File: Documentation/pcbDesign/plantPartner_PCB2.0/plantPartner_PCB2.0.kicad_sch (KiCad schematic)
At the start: 52 parts, among them IC1 MPM3610, J1 Conn_01x04, J11 Conn_01x02, J16 Conn_01x04, J17 Conn_01x03, J2 Conn_01x04, J20 Conn_02x04_Top_Bottom, J21 Conn_01x04, J22 Conn_01x04, J23 Conn_01x01, J24 Conn_01x03, J25 Conn_01x03, J26 Conn_01x01, J27 Conn_01x01, J28 Conn_01x01, J29 Conn_01x02, J3 Conn_01x04, J30 Screw_Terminal_01x02, J4 Screw_Terminal, J5 Conn_01x02, J6 Barrel_Jack, J7 Screw_Terminal_01x02, J8 Conn_02x04_Top_Bottom, Q4 AO3400A, U2 MAX485, U3 ESP32-DEVKIT-V1

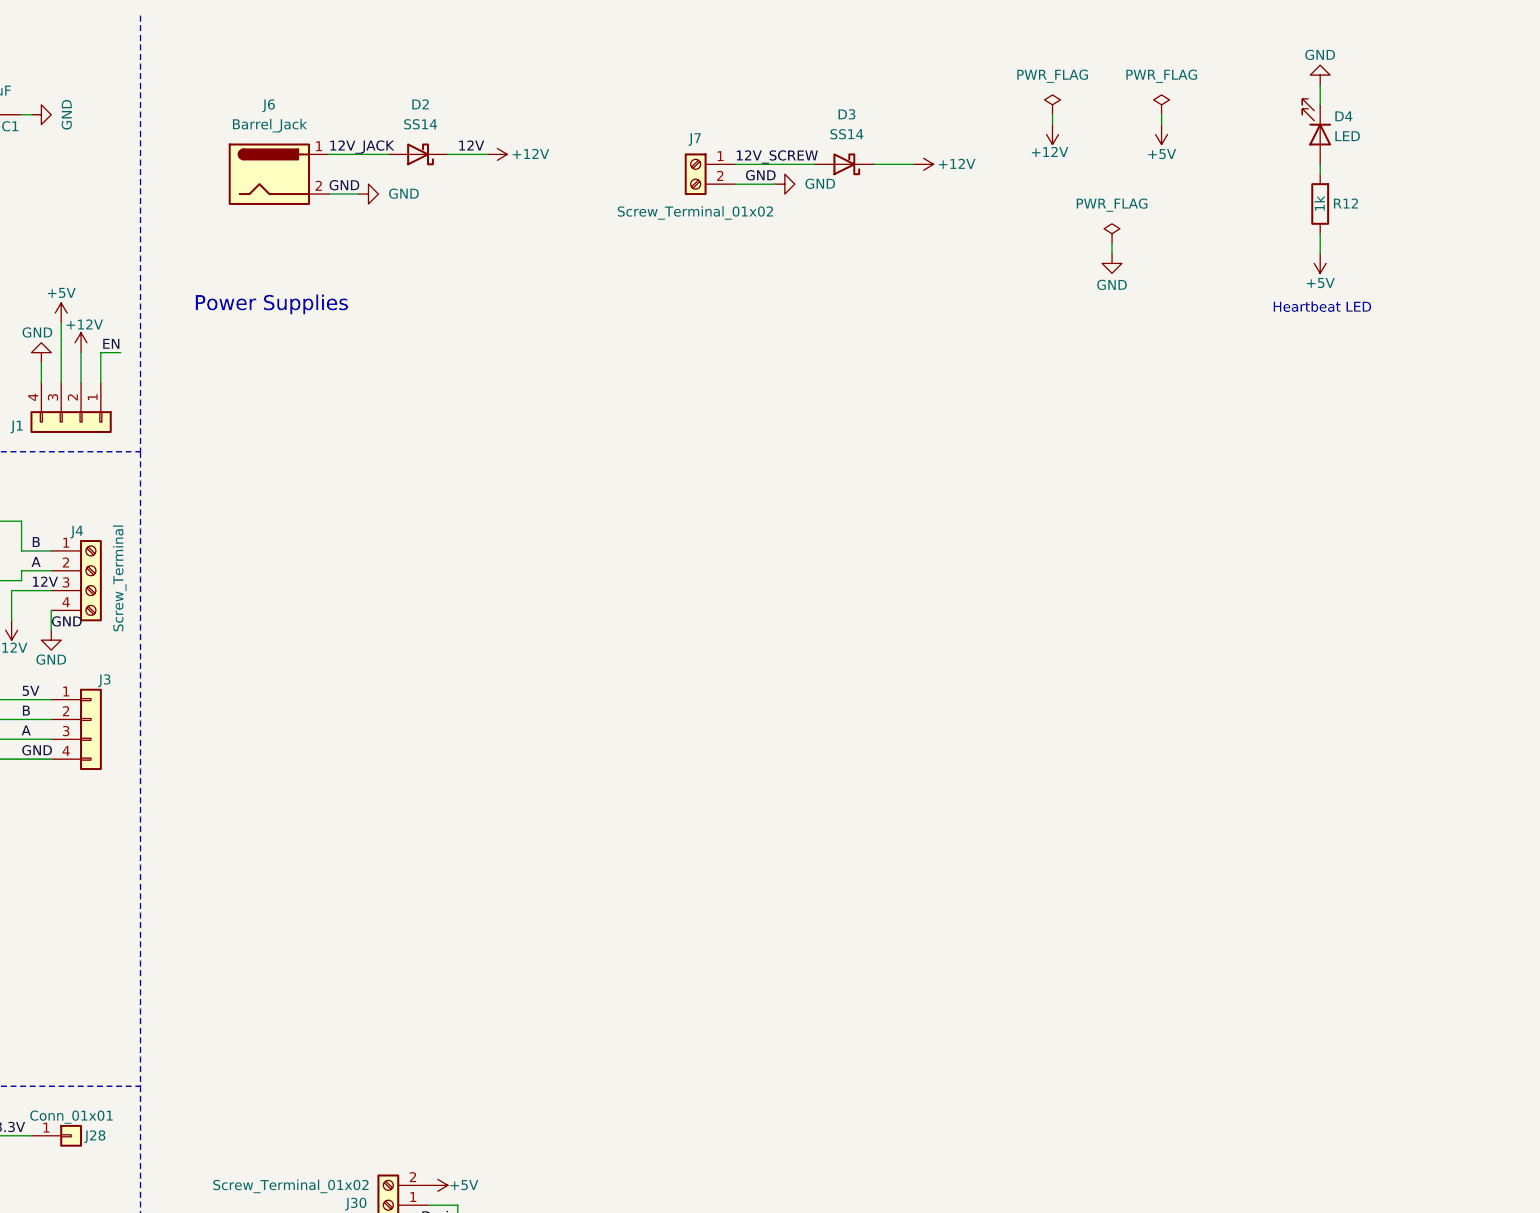
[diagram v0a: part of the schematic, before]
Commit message: Added basic implementation of 2.0 changes to see how much cheaper new PCB would be. As of now, it is half the price :O
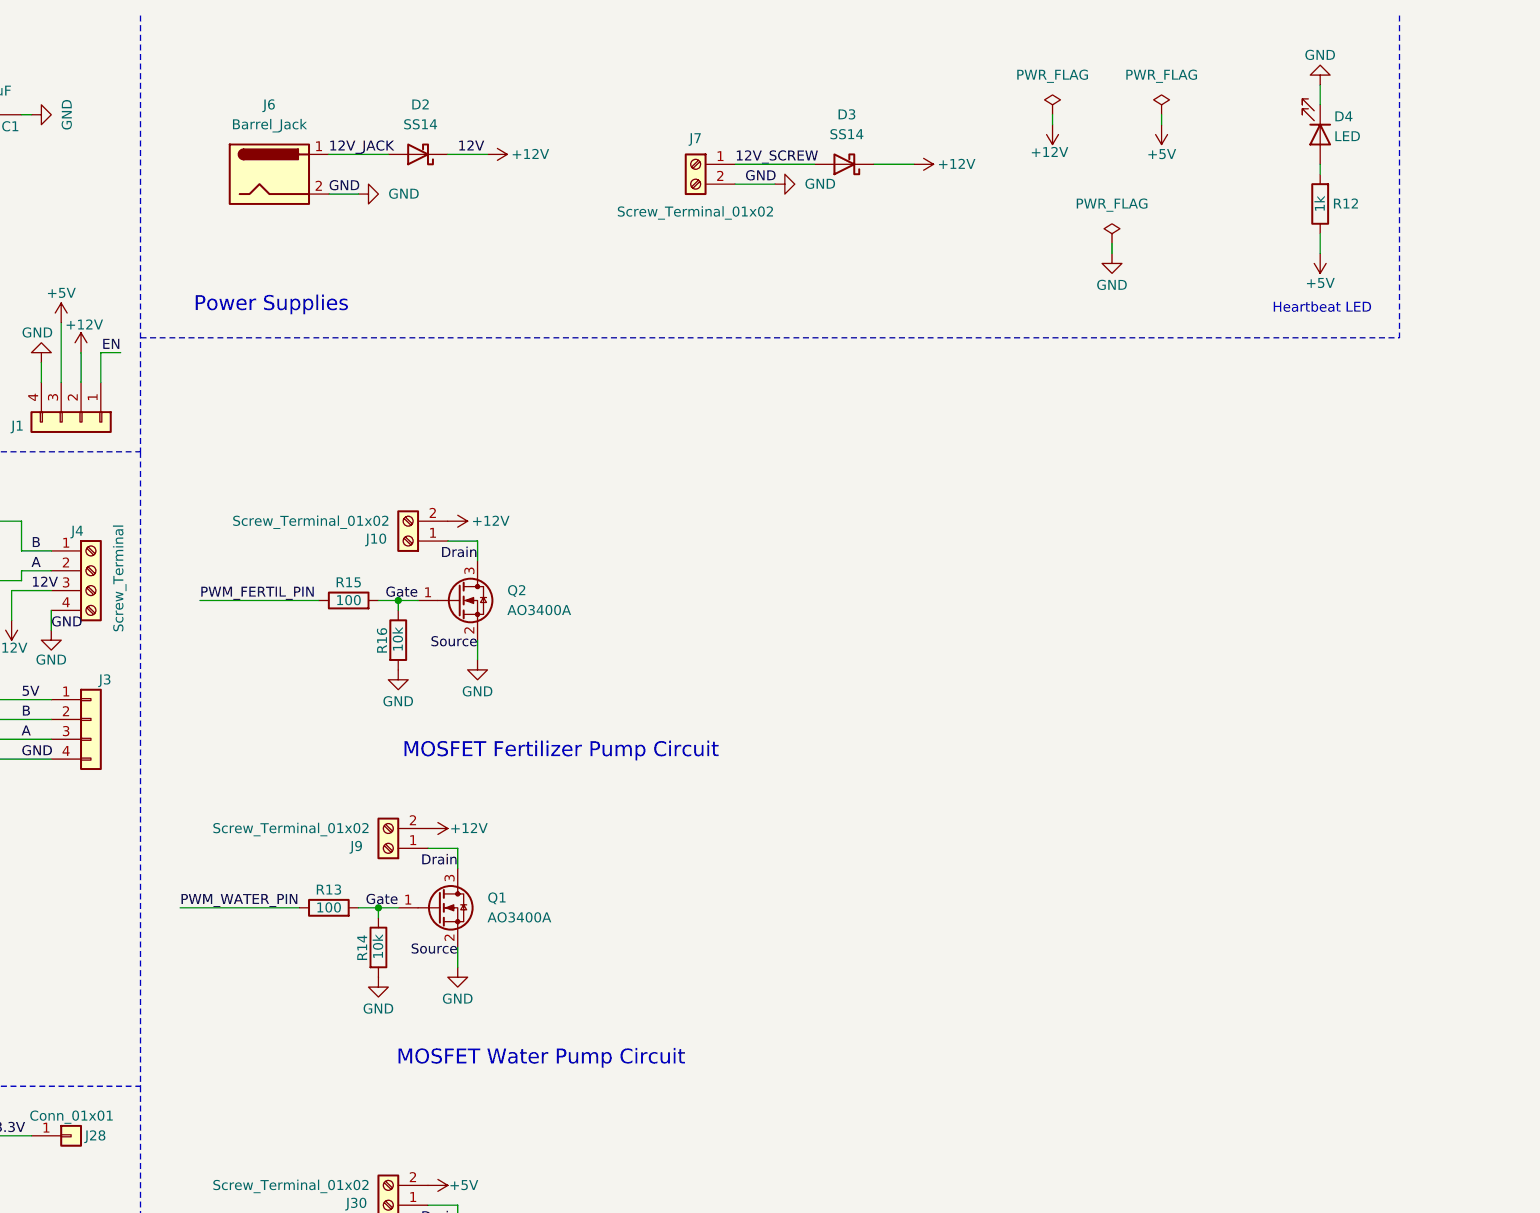
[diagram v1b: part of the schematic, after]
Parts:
- added J10, J9: Screw_Terminal_01x02, TerminalBlock_Phoenix:TerminalBlock_Phoenix_MPT-0,5-2-2.54_1x02_P2.54mm_Horizontal, symbol Connector:Screw_Terminal_01x02
- added Q1, Q2: AO3400A, Package_TO_SOT_SMD:SOT-23, symbol Transistor_FET:AO3400A
- added R13, R15: 100, Resistor_SMD:R_0402_1005Metric, symbol Device:R
- added R14, R16: 10k, Resistor_SMD:R_0402_1005Metric, symbol Device:R
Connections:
- net +12V: now also J10.2 (Pin_2), J9.2 (Pin_2)
- net Drain: now also J10.1 (Pin_1), J9.1 (Pin_1), Q1.3 (D), Q2.3 (D)
- net GND: now also Q1.2 (S), Q2.2 (S), R14.2, R16.2
- net Gate: now also Q1.1 (G), Q2.1 (G), R13.2, R14.1, R15.2, R16.1
- net PWM_FERTIL_PIN: now also R15.1
- net PWM_WATER_PIN: now also R13.1
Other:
- note added: "MOSFET Fertilizer Pump Circuit"
- note added: "MOSFET Water Pump Circuit"

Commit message: Cleaning up MOSFET circuits
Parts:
- added C5, C6: 220uF, Capacitor_SMD:C_0603_1608Metric, symbol Device:C
- added D5, D6: SS14, Diode_SMD:D_SMA, symbol Device:D_Schottky
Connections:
- net +12V: no longer J10.2 (Pin_2), J9.2 (Pin_2)
- net +5V: now also J10.2 (Pin_2), J9.2 (Pin_2), C5.1, C6.1, D5.1 (K), D6.1 (K)
- net Drain: now also D5.2 (A), D6.2 (A)
- net GND: now also C5.2, C6.2
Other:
- note removed: "Terminal Blocks Needed: 2 Pin - 2 * 5 = 10 3 Pin - 2 * 5 = 10 4 Pin - 1 * 5 = 5"
- moved on the sheet: C1, C2, C3, C4, D1, D10, D2, D3, D4, IC1, J1, J10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

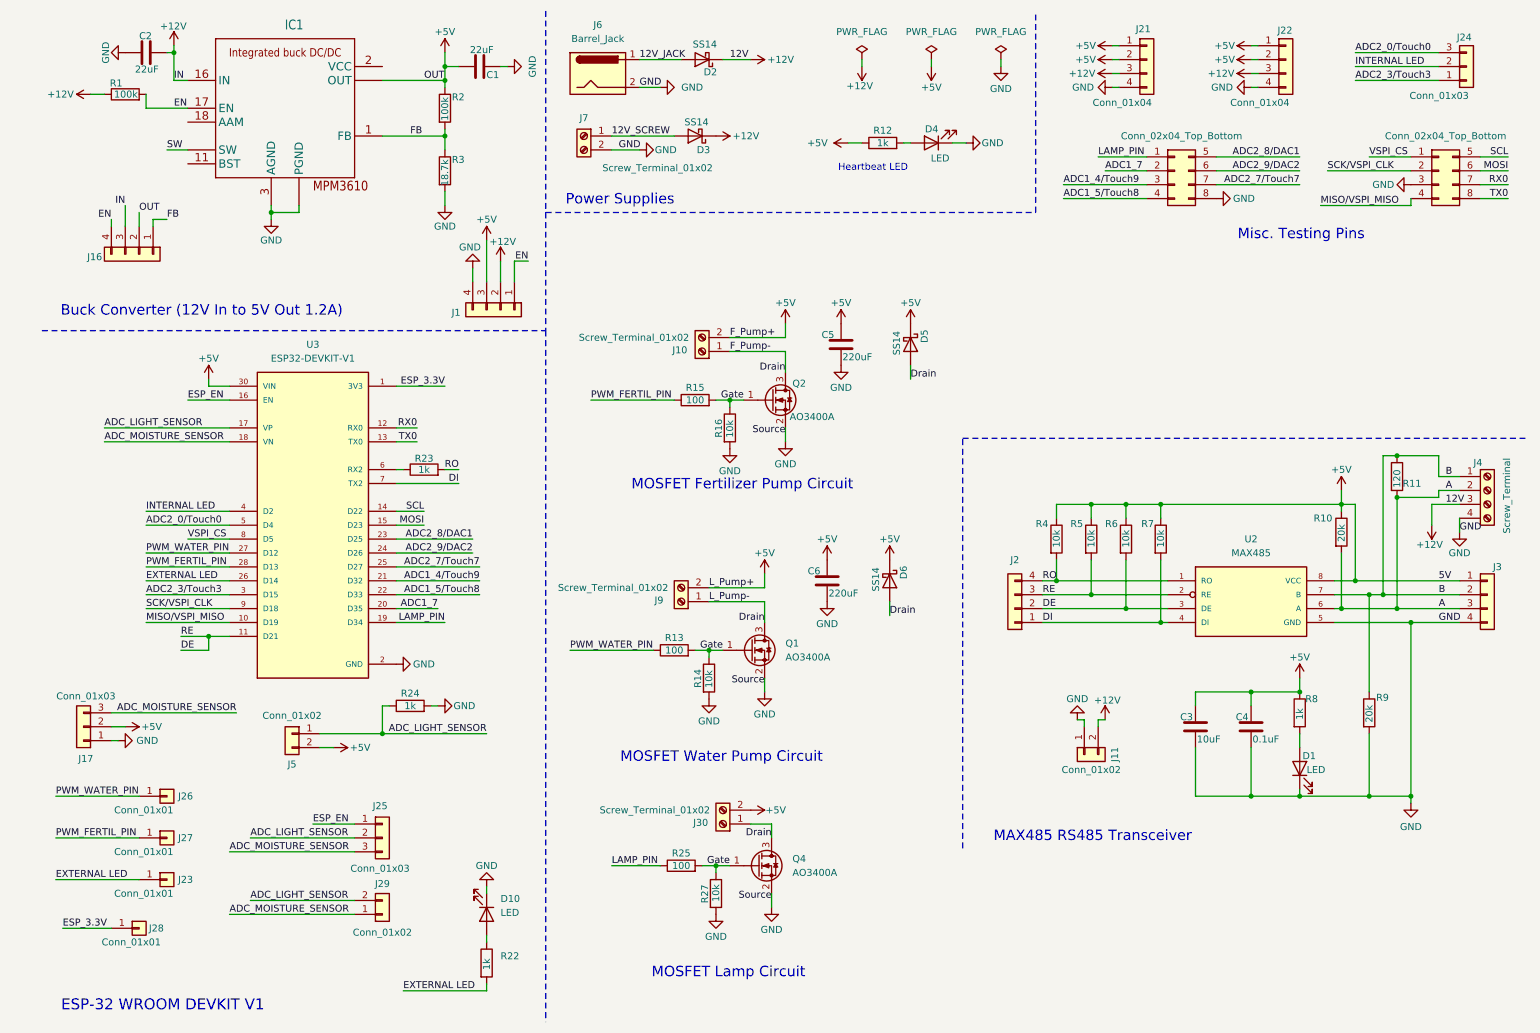
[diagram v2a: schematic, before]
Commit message: I still need to test MOSFET circuits in Ltspice but I cleaned up the v2 Schematic and starting routing v2 PCB
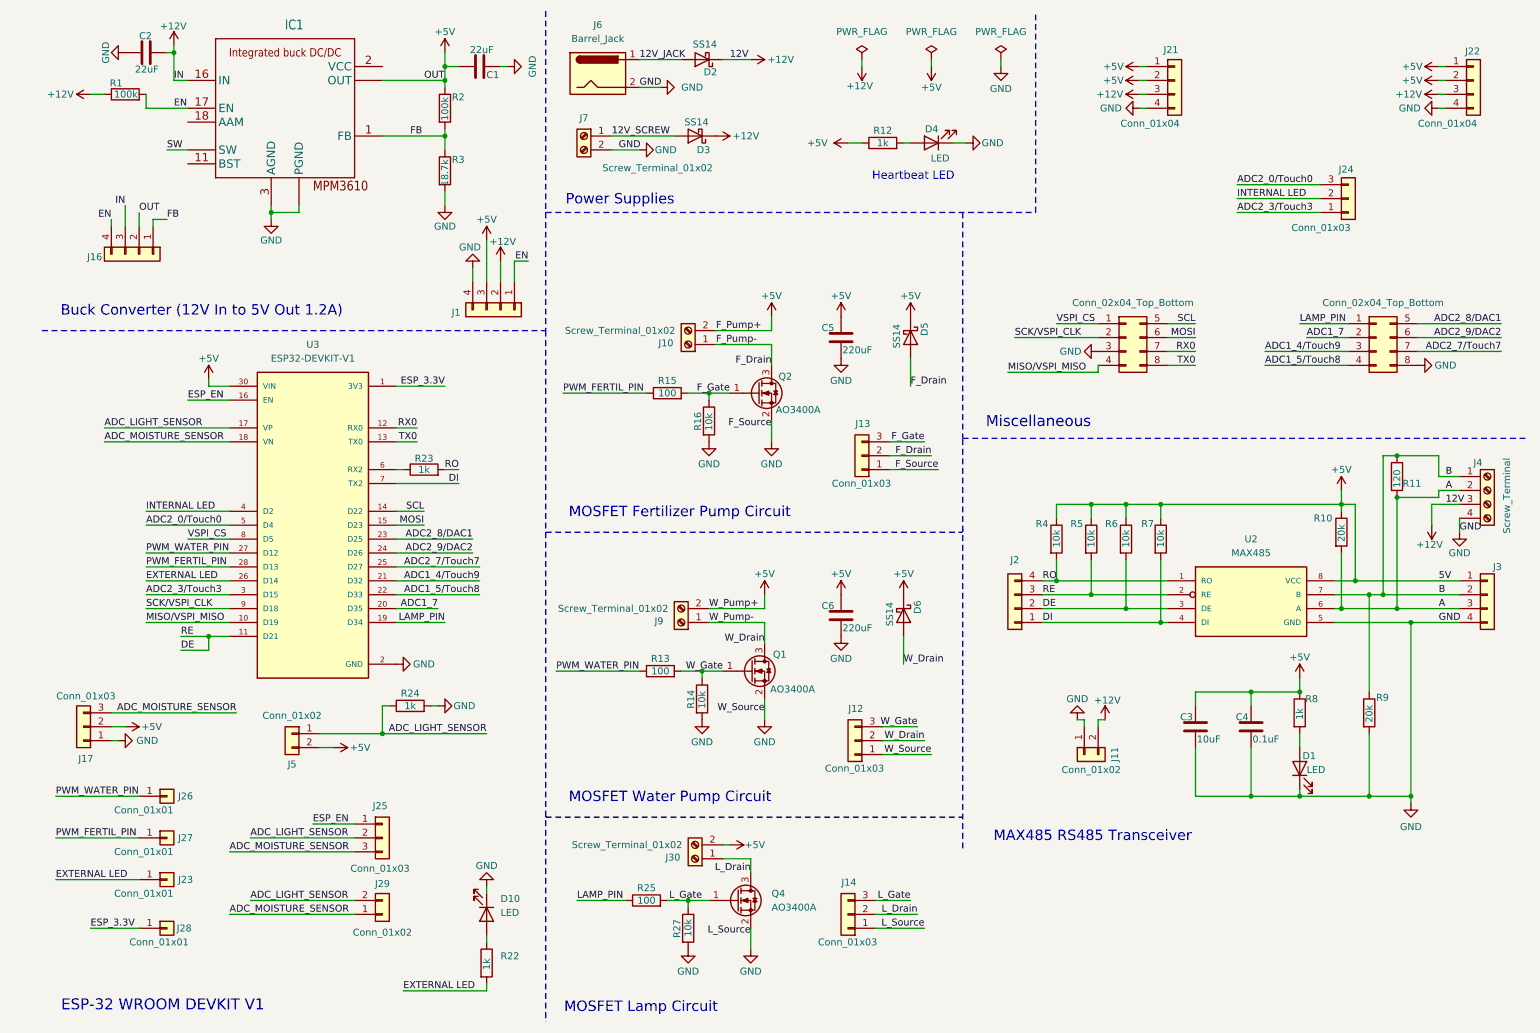
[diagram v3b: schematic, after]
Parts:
- added J12, J13, J14: Conn_01x03, Connector_PinHeader_2.54mm:PinHeader_1x03_P2.54mm_Vertical, symbol Connector_Generic:Conn_01x03
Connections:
- net GND: now also J12.1 (Pin_1), J13.1 (Pin_1), J14.1 (Pin_1)
- removed net Drain: D5.2 (A), D6.2 (A), J10.1 (Pin_1), J30.1 (Pin_1), J9.1 (Pin_1), Q1.3 (D), Q2.3 (D), Q4.3 (D)
- removed net Gate: Q1.1 (G), Q2.1 (G), Q4.1 (G), R13.2, R14.1, R15.2, R16.1, R25.2, R27.1
- new net F_Drain: D5.2 (A), J10.1 (Pin_1), J13.2 (Pin_2), Q2.3 (D)
- new net F_Gate: J13.3 (Pin_3), Q2.1 (G), R15.2, R16.1
- new net L_Drain: J14.2 (Pin_2), J30.1 (Pin_1), Q4.3 (D)
- new net L_Gate: J14.3 (Pin_3), Q4.1 (G), R25.2, R27.1
- new net W_Drain: D6.2 (A), J12.2 (Pin_2), J9.1 (Pin_1), Q1.3 (D)
- new net W_Gate: J12.3 (Pin_3), Q1.1 (G), R13.2, R14.1
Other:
- note added: "Miscellaneous"
- note removed: "Misc. Testing Pins"
- company: (none) -> PCB & Schematic Design by Carter Kreis
- title: (none) -> Plant Partner PCB v2
- moved on the sheet: C5, C6, D5, D6, J10, J21, J22, J24, J28, J30, J9, Q1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
